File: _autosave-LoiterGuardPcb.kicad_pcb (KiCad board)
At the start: 6 copper layers, 90 x 80 mm, 198 parts, among them IC1 SI4435DYPBF, IC2 SI4435DYPBF, IC3 KTA1170GVAE-TB, J1 B3B-XH-A, J10 878980204, J11 B16B-PH-SM4-TB_LF__SN_, J12 532610971, J2 ARJM11D7-114-AB-EW2, J3 B6B-PH-SM4-TB, J4 B2B-PH-K-S, J5 5033981892, J6 B2B-PH-K-S, J7 B6B-PH-SM4-TB, J8 B2B-PH-K-S, J9 B2B-PH-K-S, Q1 MBT3904DW1, Q2 BSS138, Q3 PDTC114EU_115, Q4 PDTC114EU_115, Q5 PDTC114EU_115, Q6 AO3400A, Q7 AO3400A, U1 TPS2378DDAR(HSOIC-8), U10 NL-SW-LTE-TC4NAG-B, U11 74AHC1G08, U12 MCP23017_ML, U13 DFR0299, U2 LMR33630ADDAR, U3 TX4138(ESOIC-8), U4 TX4138(ESOIC-8), U5 AP62201Z6-7, U6 AP62201Z6-7, U7 W5500, U8 ESP32-S3-WROOM-1-N16R8, U9 TPL5010

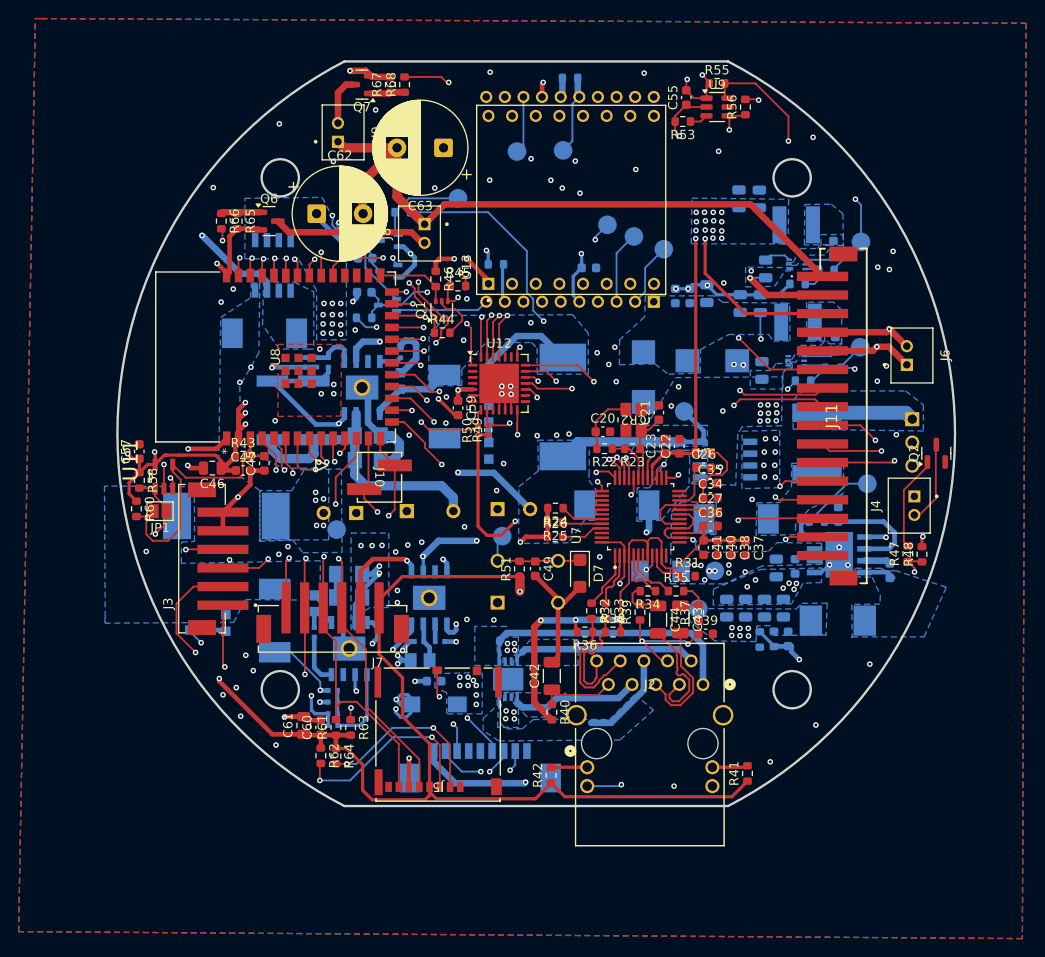
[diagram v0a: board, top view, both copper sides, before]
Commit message: WIP - starting moving reference silkscreens around
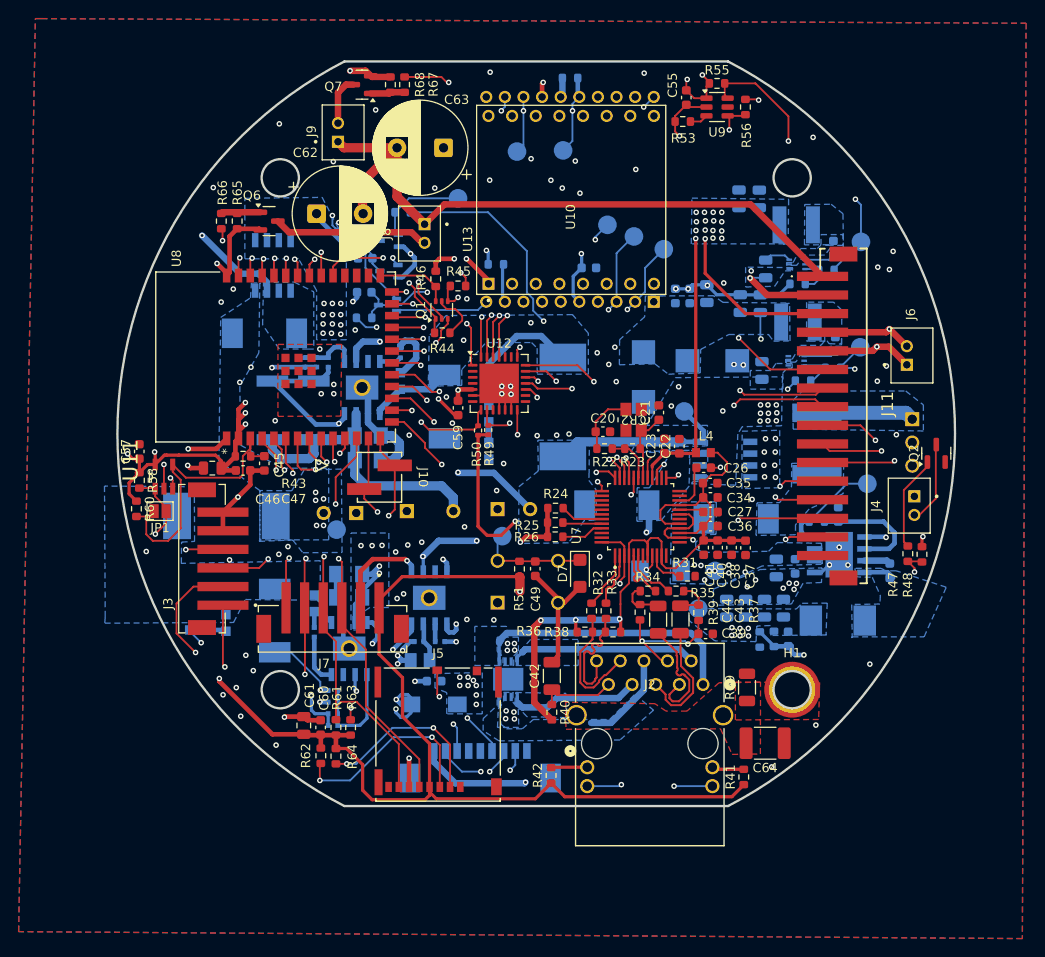
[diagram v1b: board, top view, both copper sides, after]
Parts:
- added C64: 2.2nF, Capacitor_SMD:C_1812_4532Metric, F.Cu at (167.1, 124.0)
- added H1: MountingHole_Pad, MountingHole:MountingHole_3mm_Pad_TopOnly, F.Cu at (170.0, 118.3)
- added R69: 1M, Resistor_SMD:R_1206_3216Metric, F.Cu at (165.2, 118.0)
- moved R41 0.55 mm to (164.8, 127.7)
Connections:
- J2 pad 15: (no net) -> GNDPWR
- J2 pad 16: (no net) -> GNDPWR
- U1 pad 6: /MCU/SDA -> Net-(U1-CDB)
- U3 pad 6: /MCU/SDA -> Net-(U1-CDB)
- U4 pad 6: /MCU/SDA -> Net-(U1-CDB)
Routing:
- net /MCU/SDA: track 93.9 -> 33.3 mm, vias 8 -> 4
- net Net-(U1-CDB): track 0.00 -> 59.6 mm, vias 0 -> 4
- net /MCU/CELL_RTS: track 53.5 -> 51.7 mm, vias 3 -> 4
- net Net-(U10-STATUS): track 52.4 -> 50.9 mm, vias 3 -> 4
- net /Expander/~{IO_RST}: track 32.7 -> 31.5 mm
- net +3V3: track 312.7 -> 312.2 mm, vias 33 -> 32
- net /MCU/CELL_CTS: vias 2 -> 3
- net Net-(U10-ON_OFF): vias 3 -> 4
- net /MCU/CELL_TX: vias 2 -> 3
- net /MCU/CELL_RX: vias 2 -> 3
- added copper zone on F.Cu, net GNDPWR
